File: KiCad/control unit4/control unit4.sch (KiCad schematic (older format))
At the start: 40 parts, among them J1 Conn_01x02_Female, J2 Conn_01x03_Female, J3 Conn_01x03_Female, J4 Conn_01x02_Female, J5 Conn_01x02_Female, U1 LM358, U2 LM358

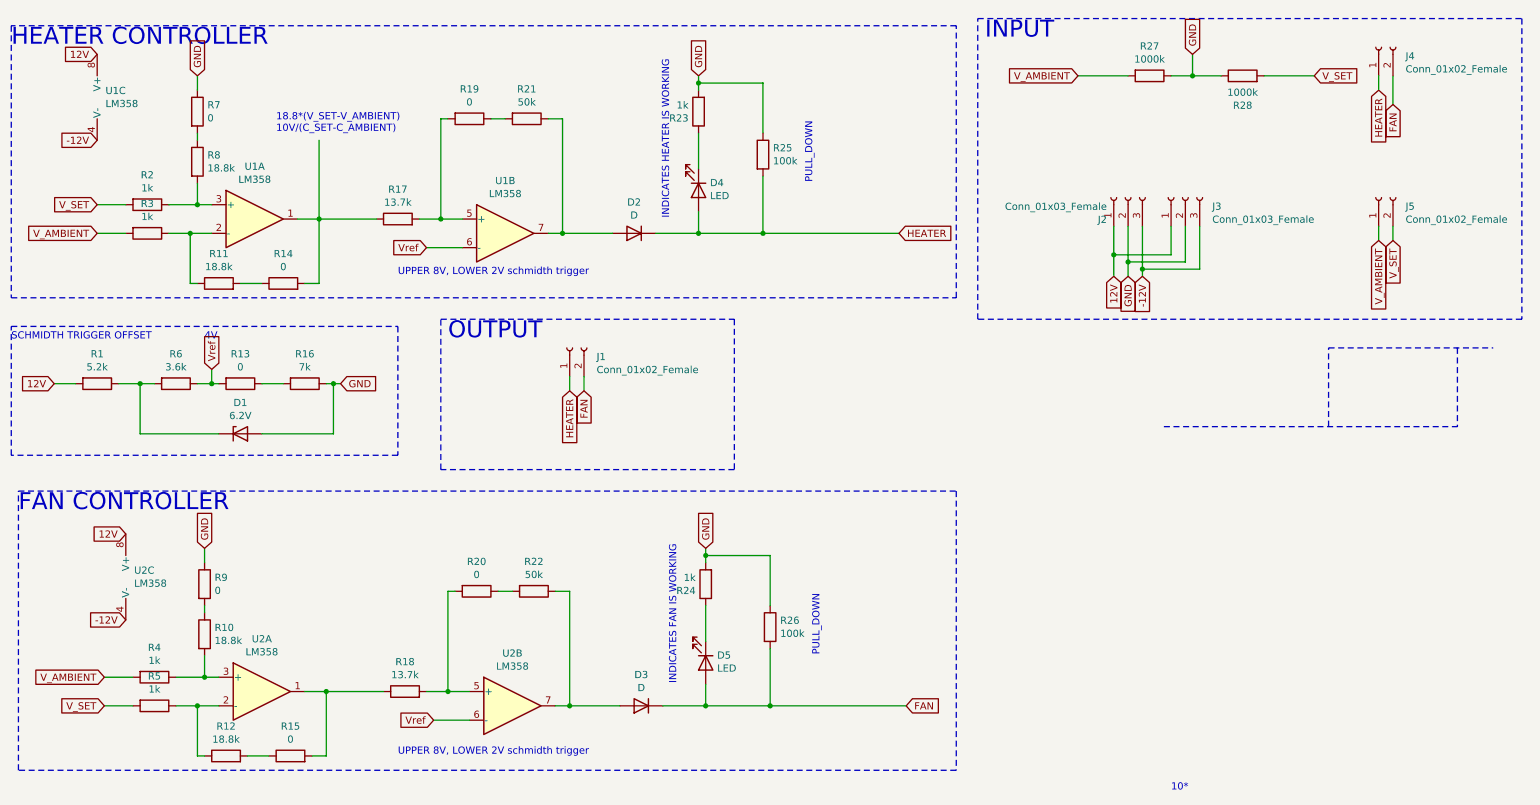
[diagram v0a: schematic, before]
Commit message: PCB of Control unit 4 is finished
.
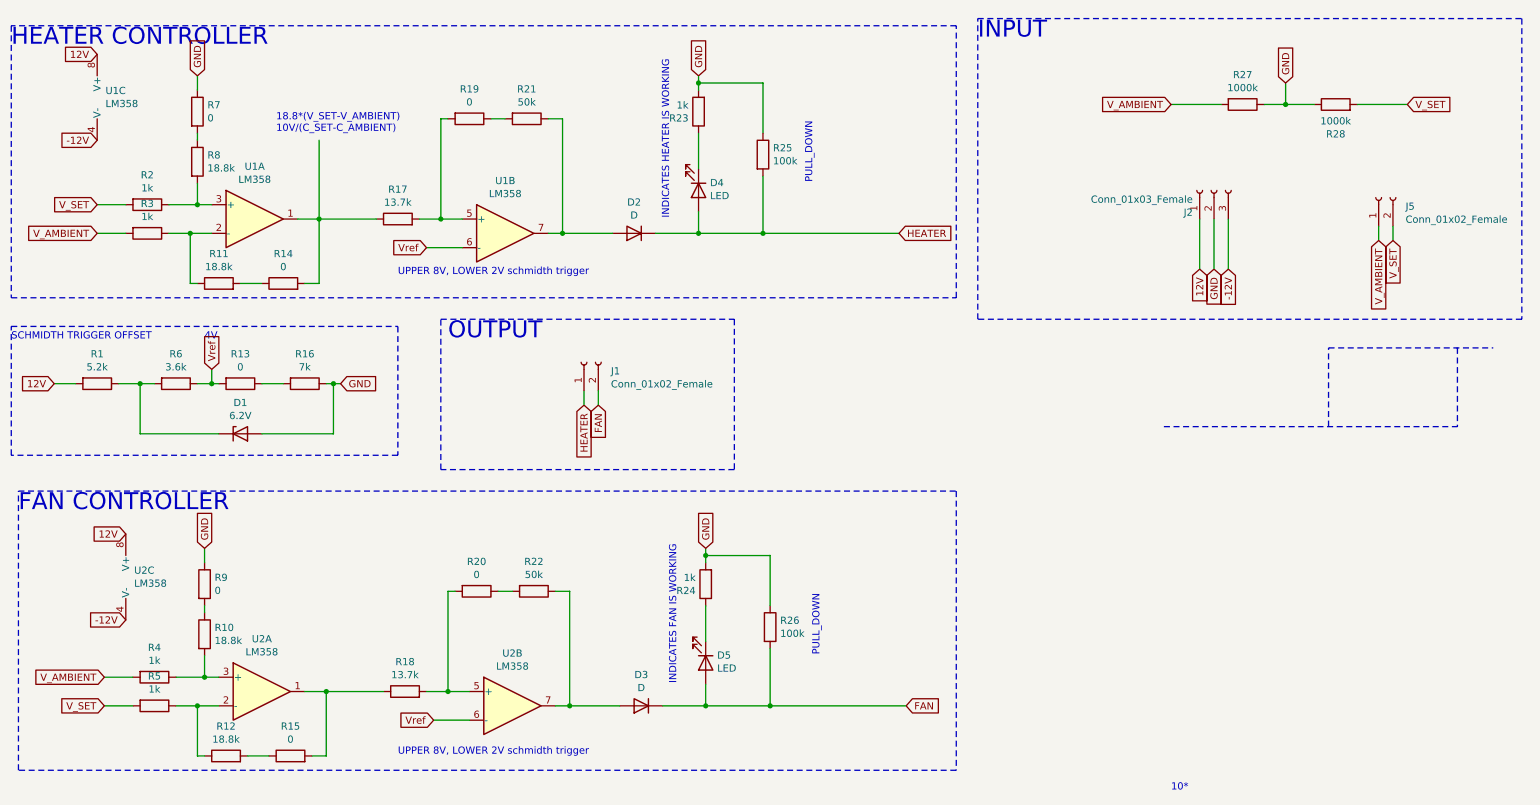
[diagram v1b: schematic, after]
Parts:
- removed J3: Conn_01x03_Female, symbol Connector:Conn_01x03_Female
- removed J4: Conn_01x02_Female, symbol Connector:Conn_01x02_Female
- D1, D2, D3: footprint (none) -> Diode_THT:D_5W_P12.70mm_Horizontal
- D4, D5: footprint (none) -> LED_THT:LED_D3.0mm_FlatTop
- J1, J5: footprint (none) -> TerminalBlock:TerminalBlock_Altech_AK300-2_P5.00mm
- J2: footprint (none) -> TerminalBlock:TerminalBlock_Altech_AK300-3_P5.00mm
- R1, R10, R11, R12, R13, R14, R15, R16, R17, R18, R19, R2, R20, R21, R22, R23, R24, R25, R26, R27, R28, R3, R4, R5, R6, R7, R8, R9: footprint (none) -> Resistor_THT:R_Axial_DIN0309_L9.0mm_D3.2mm_P12.70mm_Horizontal
- U1, U2: footprint (none) -> Package_DIP:DIP-8_W7.62mm
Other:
- moved on the sheet: J1, J2, R27, R28

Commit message: .
.
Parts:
- D4: value LED -> RED_LED
- D5: value LED -> BLUE_LED
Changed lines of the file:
@@
 P 5350 1900
 F 0 "D4" V 5297 1980 50  0000 L CNN
-F 1 "LED" V 5388 1980 50  0000 L CNN
+F 1 "RED_LED" V 5388 1980 50  0000 L CNN
 F 2 "LED_THT:LED_D3.0mm_FlatTop" H 5350 1900 50  0001 C CNN
 F 3 "~" H 5350 1900 50  0001 C CNN
@@
 P 5400 5200
 F 0 "D5" V 5347 5280 50  0000 L CNN
-F 1 "LED" V 5438 5280 50  0000 L CNN
+F 1 "BLUE_LED" V 5438 5280 50  0000 L CNN
 F 2 "LED_THT:LED_D3.0mm_FlatTop" H 5400 5200 50  0001 C CNN
 F 3 "~" H 5400 5200 50  0001 C CNN

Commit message: Final report is finished
.
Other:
- moved on the sheet: J1
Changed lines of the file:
@@
 L Connector:Conn_01x02_Female J1
 U 1 1 6209D2C4
-P 4550 3100
-F 0 "J1" V 4488 2912 50  0000 R CNN
-F 1 "Conn_01x02_Female" V 4397 2912 50  0000 R CNN
-F 2 "TerminalBlock:TerminalBlock_Altech_AK300-2_P5.00mm" H 4550 3100 50  0001 C CNN
-F 3 "~" H 4550 3100 50  0001 C CNN
-	1    4550 3100
+P 3850 3100
+F 0 "J1" V 3788 2912 50  0000 R CNN
+F 1 "Conn_01x02_Female" V 3697 2912 50  0000 R CNN
+F 2 "TerminalBlock:TerminalBlock_Altech_AK300-2_P5.00mm" H 3850 3100 50  0001 C CNN
+F 3 "~" H 3850 3100 50  0001 C CNN
+	1    3850 3100
 	0    -1   -1   0
 $EndComp
 Wire Wire Line
-	4550 3300 4550 3400
+	3850 3300 3850 3400
 Wire Wire Line
-	4650 3400 4650 3300
-Text GLabel 4550 3400 3    50   Input ~ 0
+	3950 3400 3950 3300
+Text GLabel 3850 3400 3    50   Input ~ 0
 HEATER
-Text GLabel 4650 3400 3    50   Input ~ 0
+Text GLabel 3950 3400 3    50   Input ~ 0
 FAN
 Text Notes 5200 5350 1    50   ~ 0
@@
 Text Notes 5150 2100 1    50   ~ 0
 INDICATES HEATER IS WORKING
-Wire Notes Line
-	5600 2800 5600 3850
-Wire Notes Line
-	5600 3850 3550 3850
-Wire Notes Line
-	3550 3850 3550 2800
-Wire Notes Line
-	3550 2800 5600 2800
 Text Notes 3600 2950 0    118  ~ 0
 OUTPUT
@@
 Wire Wire Line
 	9050 2100 9050 2450
+Text Notes 5800 3950 0    50   ~ 0
+UPPER 8V, LOWER 2V schmidth trigger\n
+Wire Notes Line
+	3550 3850 4950 3850
+Wire Notes Line
+	4950 3850 4950 2750
+Wire Notes Line
+	4950 2750 3550 2750
+Wire Notes Line
+	3550 2750 3550 3850
 $EndSCHEMATC
